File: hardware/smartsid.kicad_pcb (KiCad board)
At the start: 2 copper layers, 50.9 x 53.8 mm, 46 parts, among them P1 INPUT, P2 CONTROL, P3 POT2, P4 SOCKET, P5 OUTPUT, U1 GAL16V8, U2 SID2, U3 7812, U4 7809, U5 SID1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

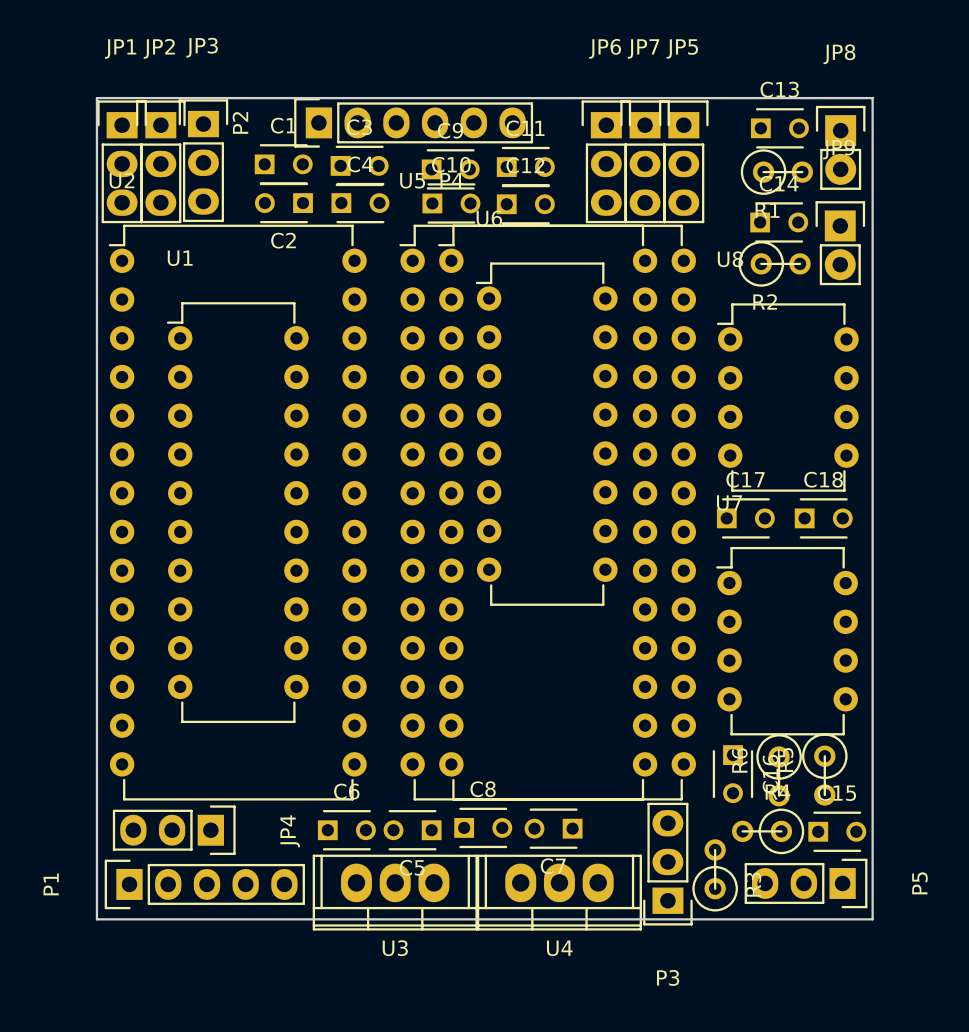
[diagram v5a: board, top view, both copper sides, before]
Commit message: Hardware: Rearranged components, first successful (auto)routing
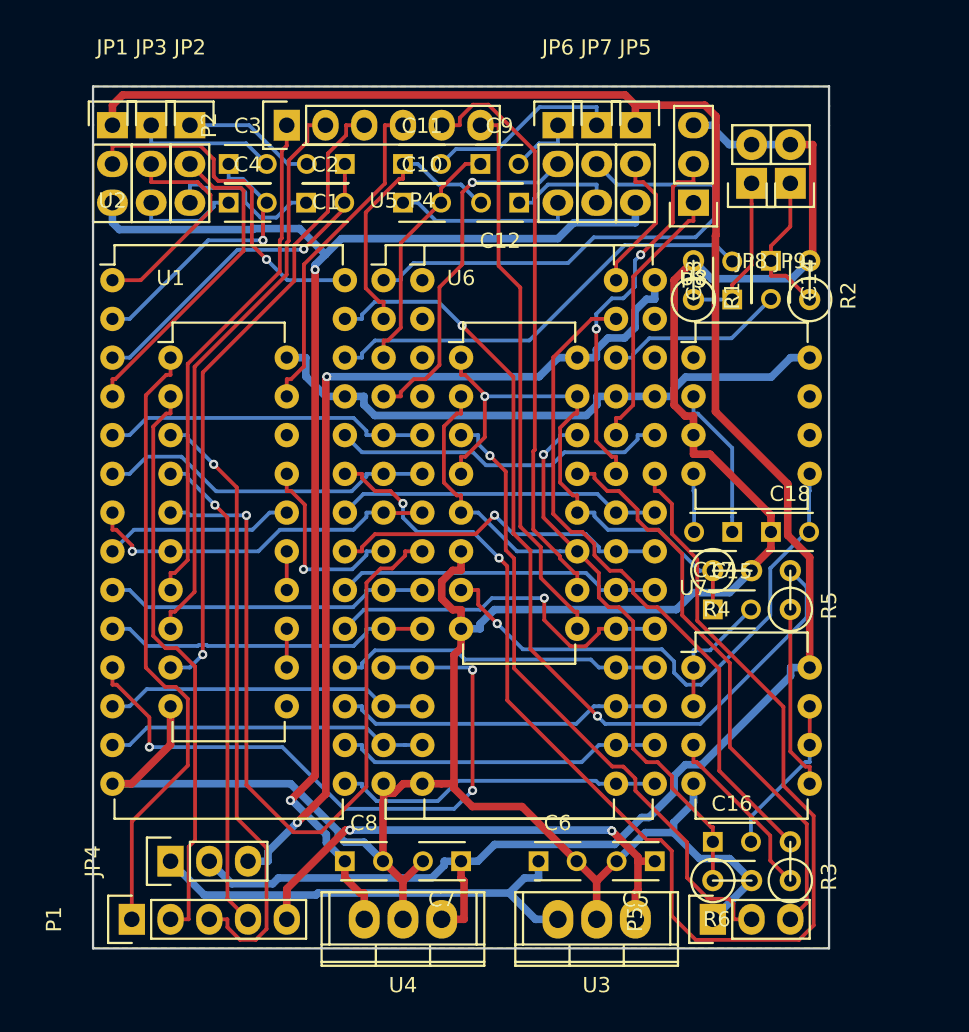
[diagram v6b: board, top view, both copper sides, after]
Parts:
- moved P3 45.8 mm to (168.9, 76.2)
- moved R4 17.2 mm to (171.4, 100.3), turned to 0 degrees
- moved C15 16.1 mm to (170.2, 102.9)
- moved C5 14.8 mm to (166.4, 119.4)
- moved C6 14.0 mm to (158.8, 119.4)
- moved U3 13.4 mm to (162.6, 123.2)
- moved R5 12.4 mm to (175.3, 101.6), turned to 90 degrees
- moved C13 11.4 mm to (171.4, 82.5), turned to 90 degrees
- moved U4 10.5 mm to (149.9, 123.2)
- moved R1 9.20 mm to (168.9, 81.3), turned to 90 degrees
- moved P5 8.83 mm to (170.2, 123.2), turned to 90 degrees
- moved C8 8.12 mm to (146.1, 119.4)
- moved C7 7.62 mm to (153.7, 119.4)
- moved R6 7.49 mm to (171.4, 120.7), turned to 0 degrees
- moved C4 7.39 mm to (138.4, 76.2)
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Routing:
- net GND: track 0.00 -> 166.1 mm
- net /+12V: track 0.00 -> 134.1 mm
- net /POTY: track 0.00 -> 86.2 mm, vias 0 -> 2
- net /+9V: track 0.00 -> 85.5 mm, vias 0 -> 2
- net VDD: track 0.00 -> 60.5 mm, vias 0 -> 2
- net /S2OUT: track 0.00 -> 58.6 mm, vias 0 -> 2
- net /RIGHT: track 0.00 -> 53.8 mm, vias 0 -> 1
- net /~CS: track 0.00 -> 51.2 mm, vias 0 -> 1
- net /S1OUT: track 0.00 -> 44.6 mm
- net /A2: track 0.00 -> 43.6 mm, vias 0 -> 3
- net /IO1EN: track 0.00 -> 42.3 mm, vias 0 -> 1
- net /RIGHT_OUT: track 0.00 -> 42.2 mm, vias 0 -> 1
- net /A5: track 0.00 -> 40.7 mm
- net /~IO1: track 0.00 -> 40.6 mm, vias 0 -> 1
- net VCC: track 0.00 -> 39.1 mm
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- added copper zone on B.Cu, net GND
- added copper zone on F.Cu, net GND
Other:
- board size 50.9 x 53.8 mm -> 48.3 x 56.5 mm

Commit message: Hardware: Added some proper pinheaders, new routing, added more docs
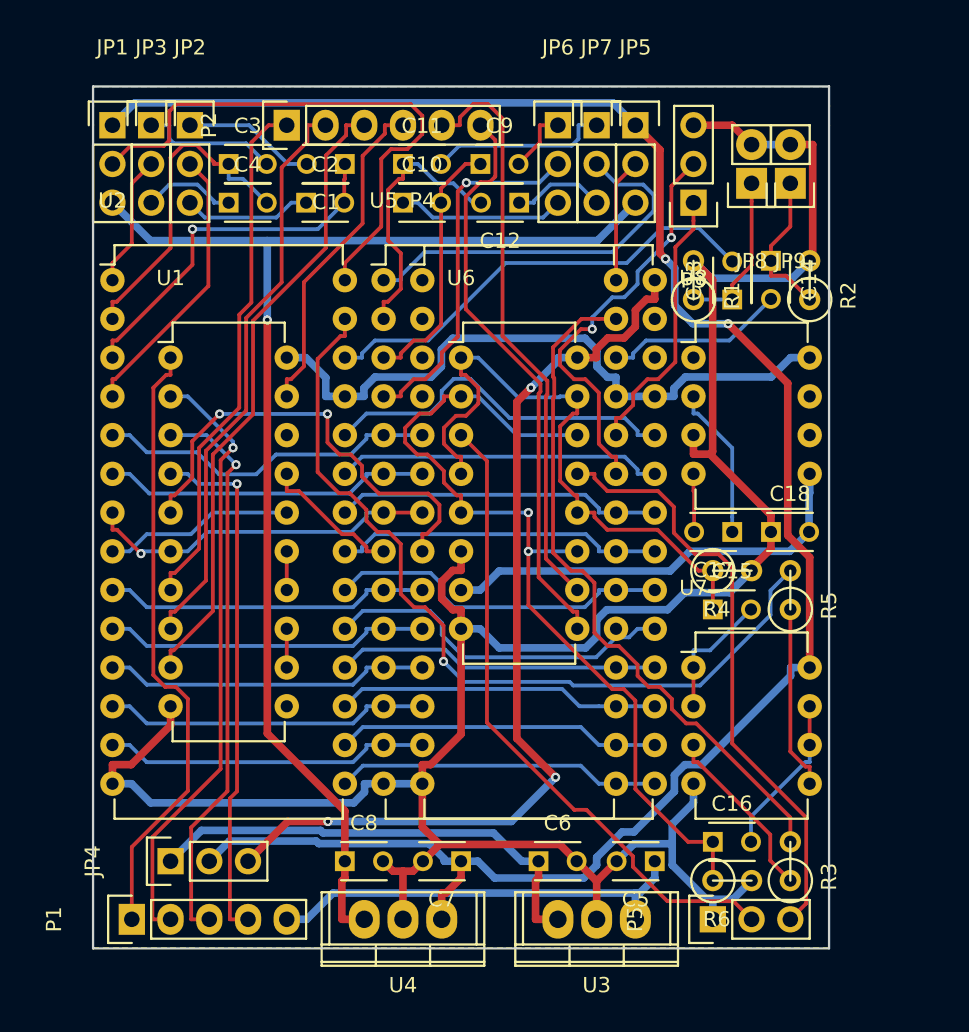
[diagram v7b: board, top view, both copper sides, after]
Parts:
- JP1, JP2, JP3, JP4, JP5, JP6, JP7, P3, P5: footprint Pin_Headers:Pin_Header_Straight_1x03 -> Pinheaders:Pin_Header_Straight_1x03
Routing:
- net /POTY: track 86.2 -> 21.4 mm, vias 2 -> 0
- net /A2: track 43.6 -> 21.4 mm, vias 3 -> 0
- net /~CS: track 51.2 -> 30.0 mm, vias 1 -> 2
- net Net-(JP1-Pad2): track 22.9 -> 36.9 mm, vias 1 -> 0
- net Net-(JP7-Pad2): track 33.9 -> 25.4 mm
- net /VEE: track 36.2 -> 28.2 mm, vias 1 -> 0
- net Net-(JP3-Pad2): track 14.8 -> 8.67 mm
- net /RIGHT: track 53.8 -> 59.1 mm, vias 1 -> 2
- net /+16V: track 32.6 -> 28.1 mm, vias 2 -> 0
- net /+12V: track 134.1 -> 129.6 mm, vias 0 -> 2
- net VCC: track 39.1 -> 42.9 mm
- net /LEFT: track 37.3 -> 40.9 mm, vias 1 -> 0
- net /~CS1: track 12.8 -> 9.28 mm, vias 1 -> 0
- net /~IO1: track 40.6 -> 37.3 mm
- net /S2OUT: track 58.6 -> 55.5 mm, vias 2 -> 1
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
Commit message: Hardware: Added pullups for M0 and M1, rerouted
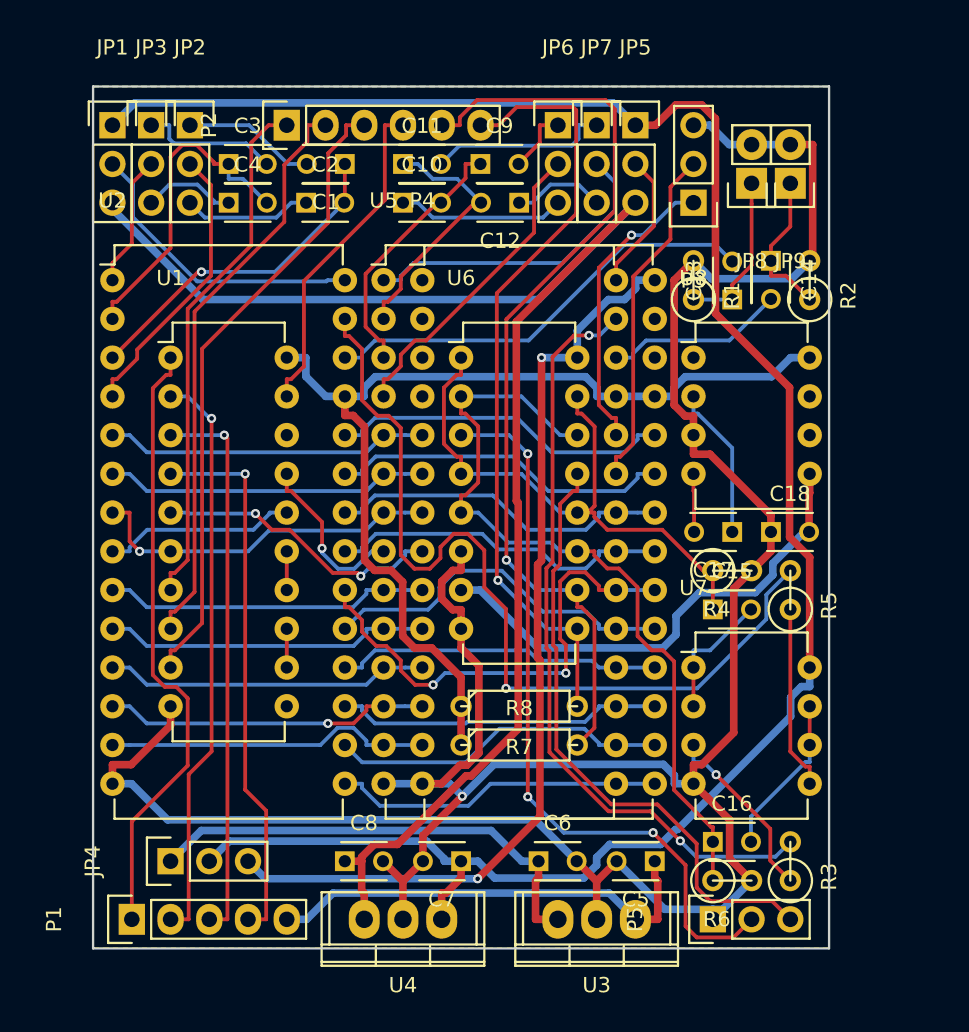
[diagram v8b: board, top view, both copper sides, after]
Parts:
- added R7: 4k7, Discret:R3, F.Cu at (157.5, 111.8)
- added R8: 4k7, Discret:R3, F.Cu at (157.5, 109.2)
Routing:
- net VCC: track 42.9 -> 66.8 mm
- net /M0: track 38.3 -> 61.8 mm, vias 0 -> 1
- net GND: track 165.7 -> 185.0 mm, vias 0 -> 1
- net Net-(JP1-Pad2): track 36.9 -> 19.7 mm
- net /M1: track 37.9 -> 51.5 mm, vias 0 -> 1
- net /+9V: track 84.5 -> 96.6 mm, vias 1 -> 0
- net /~CS: track 30.0 -> 19.1 mm
- net /D5: track 22.7 -> 32.1 mm, vias 0 -> 2
- net /RIGHT_OUT: track 42.6 -> 48.7 mm, vias 0 -> 3
- net /RIGHT: track 59.1 -> 53.1 mm, vias 2 -> 0
- net /S1OUT: track 45.5 -> 50.4 mm, vias 0 -> 2
- net Net-(JP7-Pad2): track 25.4 -> 20.8 mm
- net /POT2Y: track 27.0 -> 22.6 mm, vias 2 -> 0
- net /VEE: track 28.2 -> 32.5 mm
- net /+12V: track 129.6 -> 133.2 mm, vias 2 -> 0
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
